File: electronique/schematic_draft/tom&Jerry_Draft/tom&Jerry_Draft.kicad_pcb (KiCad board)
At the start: 4 copper layers, 54 x 57 mm, 163 parts, among them IC1101 NCS199A2RSQT2G, IC301 TCA9555RTWR, IC901 NCS199A2RSQT2G, J1001 FTSH-105-01-F-DV-P-TR, J1301 Conn_01x02, J1401 Conn_01x02, J1501 Conn_01x02, J1601 Conn_01x02, J1601 Conn_02x05_Odd_FEMALE, J1602 Conn_02x05_Odd_FEMALE, J1603 Conn_02x05_Odd_FEMALE, J201 Interrupteur, J202 USB_C_Receptacle_USB2.0_16P, J203 Conn_01x02, J204 Conn_01x02, J301 Conn_01x08, J401 Conn_01x06, J402 Conn_01x06, J501 Conn_ST_STDC14, J601 Conn_01x03, J701 Conn_02x05_Odd_FEMALE, J701 FTSH-105-01-F-DV-P-TR, J702 Conn_02x05_Odd_FEMALE, J703 Conn_02x05_Odd_FEMALE, Q201 PMOS, SW501 SW_Push, SW502 SW_Push, SW503 SW_Push, U1101 ZXBM5210-S, U201 MP1475DJ-LF-P, U202 BQ25172DSGR, U301 ADXL343, U501 STM32G431CBU6, U601 PAM8302AAY, U801 LP5812ADSDR, U901 ZXBM5210-S, Y501 16MHz

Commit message: Corrections mineures routage - PCB V2.0
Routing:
- net /Périphériques/TOF3_GPIO1: track 2.00 -> 11.1 mm, vias 1 -> 2
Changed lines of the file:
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@@
 		(tags "resistor")
 		(property "Reference" "R206"
-			(at 0 -1.17 360)
+			(at 0 -1.17 0)
 			(layer "F.SilkS")
 			(effects
@@
 		)
 		(property "Value" "40.2k"
-			(at 0 1.17 360)
+			(at 0 1.17 0)
 			(layer "F.Fab")
 			(effects
@@
 		)
 		(fp_text user "${REFERENCE}"
-			(at 0 0 360)
+			(at 0 0 0)
 			(layer "F.Fab")
 			(effects
@@
 		(tags "capacitor")
 		(property "Reference" "C604"
-			(at 0 -1.43 360)
+			(at 0 -1.43 0)
 			(layer "F.SilkS")
 			(effects
@@
 		)
 		(fp_text user "${REFERENCE}"
-			(at 0 0 360)
+			(at 0 0 0)
 			(layer "F.Fab")
 			(effects
@@
 		(at 117.1 109.3)
 		(property "Reference" "U202"
-			(at 0.925 -2.385 360)
+			(at 0.925 -2.385 0)
 			(layer "F.SilkS")
 			(effects
@@
 		)
 		(property "Value" "BQ25172DSGR"
-			(at 6.64 2.385 360)
+			(at 6.64 2.385 0)
 			(layer "F.Fab")
 			(effects
@@
 		)
 		(property "Footprint" "Tom&Jerry:IC_BQ25172DSGR"
-			(at 0 0 360)
+			(at 0 0 0)
 			(layer "F.Fab")
 			(hide yes)
@@
 		)
 		(property "Datasheet" ""
-			(at 0 0 360)
+			(at 0 0 0)
 			(layer "F.Fab")
 			(hide yes)
@@
 		)
 		(property "Description" ""
-			(at 0 0 360)
+			(at 0 0 0)
 			(layer "F.Fab")
 			(hide yes)
@@
 		(tags "capacitor")
 		(property "Reference" "C605"
-			(at 0 -1.16 360)
+			(at 0 -1.16 0)
 			(layer "F.SilkS")
 			(effects
@@
 		)
 		(fp_text user "${REFERENCE}"
-			(at 0 0 360)
+			(at 0 0 0)
 			(layer "F.Fab")
 			(effects
@@
 		(tags "capacitor")
 		(property "Reference" "C211"
-			(at 0 -1.16 360)
+			(at 0 -1.16 0)
 			(layer "F.SilkS")
 			(effects
@@
 		)
 		(property "Value" "10n"
-			(at 0 1.16 360)
+			(at 0 1.16 0)
 			(layer "F.Fab")
 			(effects
@@
 		)
 		(fp_text user "${REFERENCE}"
-			(at 0 0 360)
+			(at 0 0 0)
 			(layer "F.Fab")
 			(effects
@@
 		(tags "resistor")
 		(property "Reference" "R208"
-			(at 0 -1.17 360)
+			(at 0 -1.17 0)
 			(layer "F.SilkS")
 			(effects
@@
 		)
 		(property "Value" "15k"
-			(at 0 1.17 360)
+			(at 0 1.17 0)
 			(layer "F.Fab")
 			(effects
@@
 		)
 		(fp_text user "${REFERENCE}"
-			(at 0 0 360)
+			(at 0 0 0)
 			(layer "F.Fab")
 			(effects
@@
 	)
 	(segment
+		(start 100.075158 62.949685)
+		(end 100.54 63.414527)
+		(width 0.2)
+		(layer "F.Cu")
+		(net 38)
+	)
+	(segment
 		(start 92.800001 65.148528)
 		(end 93.824266 64.124263)
@@
 	)
 	(segment
+		(start 100.54 63.414527)
+		(end 100.54 65.165)
+		(width 0.2)
+		(layer "F.Cu")
+		(net 38)
+	)
+	(segment
 		(start 92.800001 65.7)
 		(end 92.800001 65.148528)
@@
 		(net 38)
 	)
+	(via
+		(at 100.075158 62.949685)
+		(size 0.6)
+		(drill 0.3)
+		(layers "F.Cu" "B.Cu")
+		(net 38)
+	)
+	(segment
+		(start 94.107109 64.124263)
+		(end 93.824266 64.124263)
+		(width 0.2)
+		(layer "B.Cu")
+		(net 38)
+	)
+	(segment
+		(start 95.081687 63.149685)
+		(end 94.107109 64.124263)
+		(width 0.2)
+		(layer "B.Cu")
+		(net 38)
+	)
+	(segment
+		(start 100.075158 62.949685)
+		(end 99.875158 63.149685)
+		(width 0.2)
+		(layer "B.Cu")
+		(net 38)
+	)
+	(segment
+		(start 99.875158 63.149685)
+		(end 95.081687 63.149685)
+		(width 0.2)
+		(layer "B.Cu")
+		(net 38)
+	)
 	(segment
 		(start 98.960002 67.460002)
@@
 	)
 	(segment
-		(start 88.684744 71.275)
-		(end 87.4725 71.275)
+		(start 87.4025 71.275)
+		(end 86.4575 70.33)
 		(width 0.2)
 		(layer "F.Cu")
@@
 	)
 	(segment
-		(start 86.4575 70.26)
-		(end 86.4575 69.235)
+		(start 91.825 70.589937)
+		(end 90.614937 71.8)
 		(width 0.2)
 		(layer "F.Cu")
@@
 	)
 	(segment
-		(start 91.825 70.589937)
-		(end 90.614937 71.8)
+		(start 91.825 69.924937)
+		(end 91.825 70.589937)
 		(width 0.2)
 		(layer "F.Cu")
@@
 	)
 	(segment
-		(start 90.614937 71.8)
-		(end 89.209744 71.8)
+		(start 86.4575 70.33)
+		(end 86.4575 69.235)
 		(width 0.2)
 		(layer "F.Cu")
@@
 	)
 	(segment
-		(start 87.4725 71.275)
-		(end 86.4575 70.26)
+		(start 90.614937 71.8)
+		(end 89.209744 71.8)
 		(width 0.2)
 		(layer "F.Cu")
@@
 	)
 	(segment
-		(start 91.825 69.924937)
-		(end 91.825 70.589937)
+		(start 88.684744 71.275)
+		(end 87.4025 71.275)
 		(width 0.2)
 		(layer "F.Cu")
@@
 	)
 	(segment
-		(start 88.575 70.875)
-		(end 87.7275 70.0275)
+		(start 91.325 70.524251)
+		(end 90.449251 71.4)
 		(width 0.2)
 		(layer "F.Cu")
@@
 	)
 	(segment
-		(start 91.325 69.924937)
-		(end 91.325 70.524251)
+		(start 88.85043 70.875)
+		(end 87.975 70.875)
 		(width 0.2)
 		(layer "F.Cu")
@@
 	)
 	(segment
-		(start 88.85043 70.875)
-		(end 88.575 70.875)
+		(start 87.7275 70.6275)
+		(end 87.7275 69.235)
 		(width 0.2)
 		(layer "F.Cu")
@@
 	)
 	(segment
-		(start 89.37543 71.4)
-		(end 88.85043 70.875)
+		(start 91.325 69.924937)
+		(end 91.325 70.524251)
 		(width 0.2)
 		(layer "F.Cu")
@@
 	)
 	(segment
-		(start 91.325 70.524251)
-		(end 90.449251 71.4)
+		(start 90.449251 71.4)
+		(end 89.37543 71.4)
 		(width 0.2)
 		(layer "F.Cu")
@@
 	)
 	(segment
-		(start 90.449251 71.4)
-		(end 89.37543 71.4)
+		(start 89.37543 71.4)
+		(end 88.85043 70.875)
 		(width 0.2)
 		(layer "F.Cu")
@@
 	)
 	(segment
-		(start 91.35 69.575)
-		(end 91.35 70.239999)
+		(start 87.975 70.875)
+		(end 87.7275 70.6275)
 		(width 0.2)
 		(layer "F.Cu")
@@
 	)
 	(segment
-		(start 87.7275 70.0275)
-		(end 87.7275 69.235)
+		(start 91.35 69.575)
+		(end 91.35 70.239999)
 		(width 0.2)
 		(layer "F.Cu")
@@
 	)
 	(segment
-		(start 112.892892 69.907108)
-		(end 116.3 66.5)
-		(width 0.2)
-		(layer "F.Cu")
-		(net 76)
-	)
-	(segment
-		(start 125.01 65.9)
-		(end 125.7 66.59)
+		(start 106.607108 69.907108)
+		(end 112.892892 69.907108)
 		(width 0.2)
 		(layer "F.Cu")
@@
 	)
 	(segment
-		(start 119.72 66.5)
+		(start 119.82 66.4)
 		(end 120.32 65.9)
 		(width 0.2)
@@
 	)
 	(segment
-		(start 106.607108 69.907108)
-		(end 112.892892 69.907108)
+		(start 112.892892 69.907108)
+		(end 116.4 66.4)
 		(width 0.2)
 		(layer "F.Cu")
@@
 	)
 	(segment
-		(start 116.3 66.5)
-		(end 119.72 66.5)
+		(start 125.01 65.9)
+		(end 125.7 66.59)
+		(width 0.2)
+		(layer "F.Cu")
+		(net 76)
+	)
+	(segment
+		(start 116.4 66.4)
+		(end 119.82 66.4)
 		(width 0.2)
 		(layer "F.Cu")

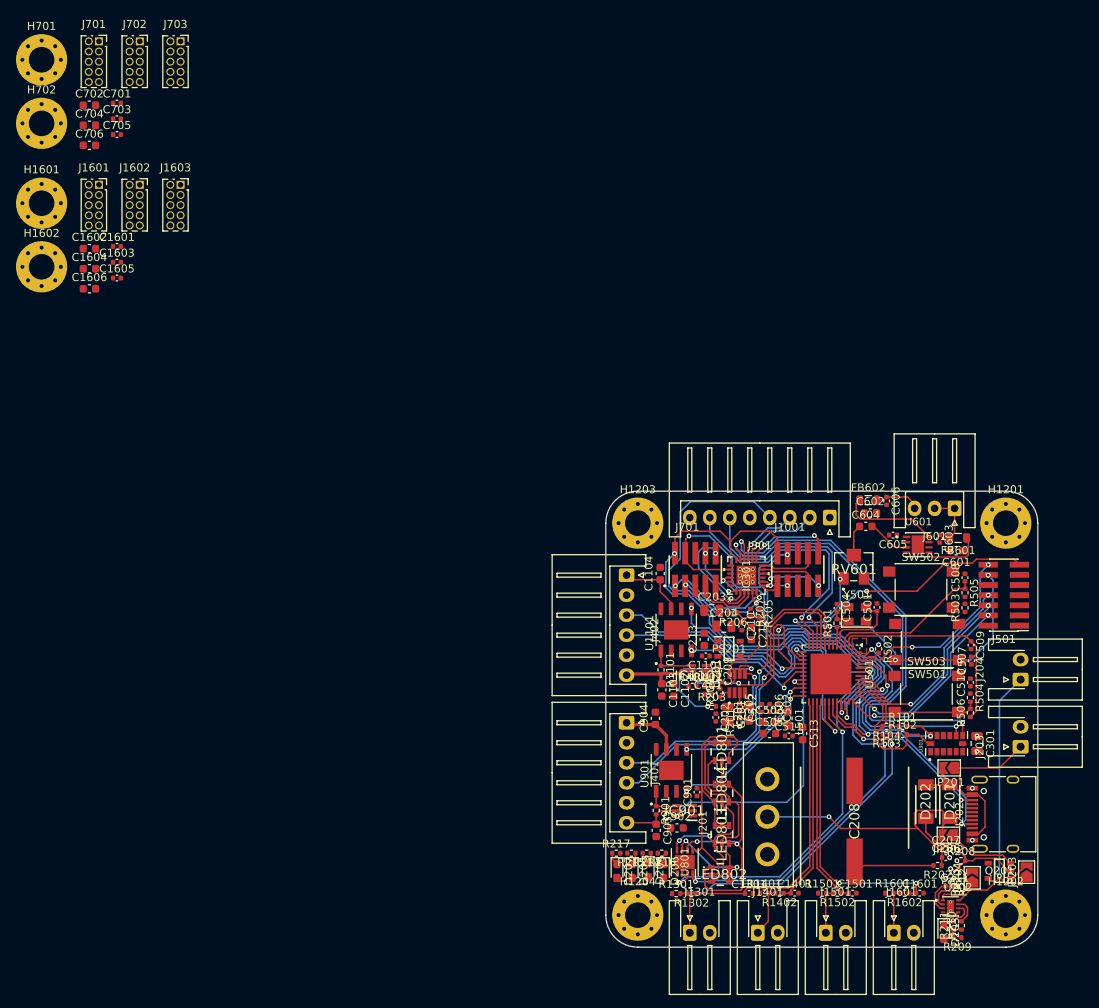
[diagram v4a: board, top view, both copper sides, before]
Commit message: Routage finish awaiting review PCB2.0
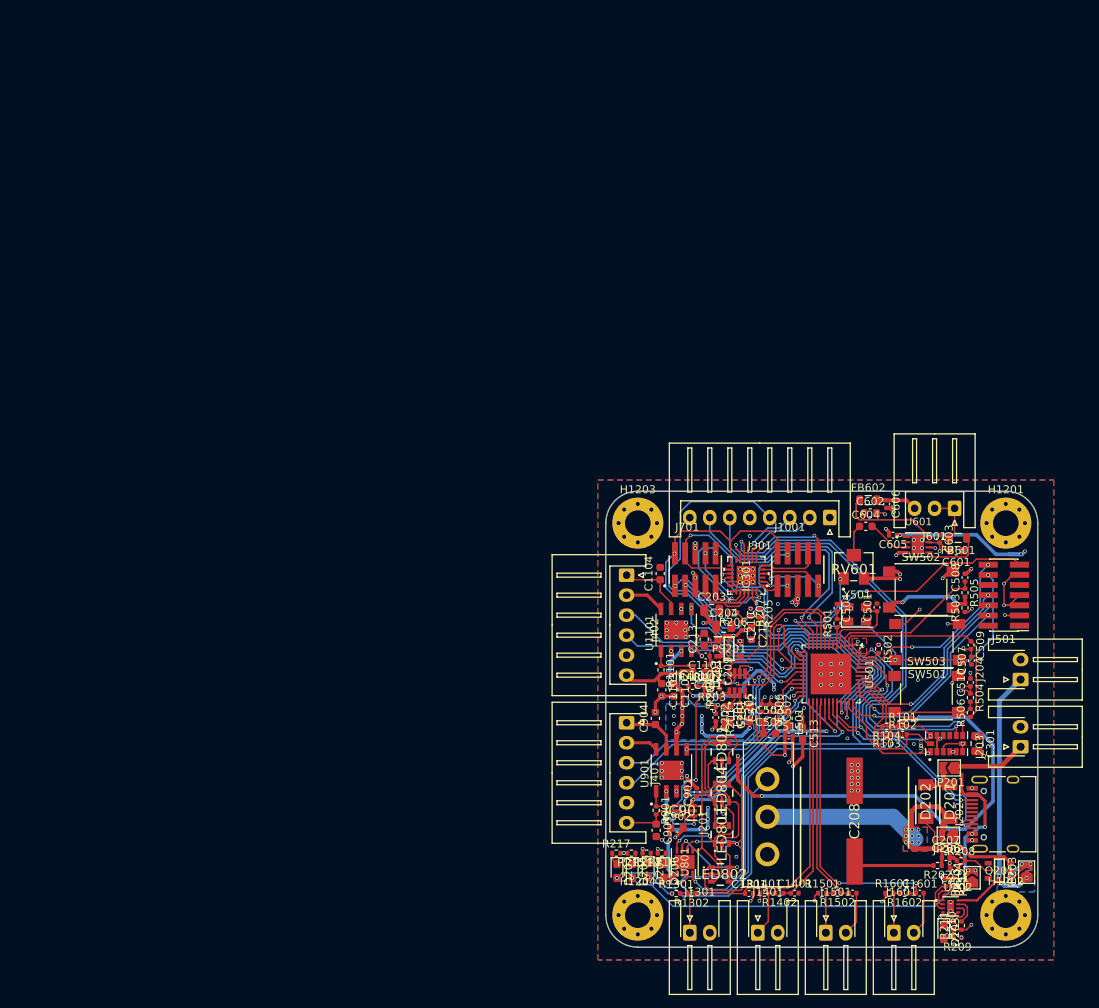
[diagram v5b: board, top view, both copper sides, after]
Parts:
- removed the C1601 at (12.9, 26.8)
- removed C1602, C1604, C1606, C702, C704, C706: 4.7uF, Capacitor_SMD:C_0603_1608Metric
- removed C1603, C1605, C701, C703, C705: 100nF, Capacitor_SMD:C_0402_1005Metric
- removed H1601, H1602, H701, H702: MountingHole_Pad, MountingHole:MountingHole_3.2mm_M3_Pad_Via
- removed the J1601 at (10.6, 19.1)
- removed J1602, J1603, J702, J703: Conn_02x05_Odd_FEMALE, Connector_PinSocket_1.27mm:PinSocket_2x05_P1.27mm_Vertical
- removed the J701 at (10.6, 1.18)
- moved C606 0.40 mm to (109.1, 59.0)
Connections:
- IC301 pad 25: (no net) -> GND
- IC301 pad V: (no net) -> GND
- U1101 pad 9: (no net) -> GND
- U601 pad 9: (no net) -> GND
- U901 pad 9: (no net) -> GND
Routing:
- net +5V: track 0.00 -> 124.4 mm, vias 0 -> 35
- net GND: track 0.00 -> 122.6 mm, vias 10 -> 104
- net +3.3V: track 0.00 -> 116.2 mm, vias 1 -> 28
- net /Alimentation/Batt_CHG: track 21.2 -> 73.0 mm, vias 0 -> 5
- net VCC: track 0.00 -> 48.6 mm, vias 0 -> 10
- net 1.65V: track 0.00 -> 25.4 mm, vias 0 -> 2
- net Net-(R503-Pad2): track 0.00 -> 12.1 mm, vias 0 -> 2
- net +3.3VA: track 2.41 -> 12.9 mm, vias 1 -> 0
- net /Motors&Drivers/ASSERV_I1: track 36.4 -> 30.5 mm
- net /Led_Debug/Led_Debug_SCL: track 148.2 -> 153.8 mm
- net /Led_Debug/Led_Debug_SDA: track 112.2 -> 117.6 mm
- net Net-(D201-K): track 35.7 -> 39.5 mm, vias 1 -> 9
- net Net-(JP203-B): track 2.69 -> 6.17 mm, vias 0 -> 3
- net /Périphériques/TOF4_GPIO1: track 12.7 -> 15.4 mm
- net /Motors&Drivers/ENCODER_2A: track 41.4 -> 40.0 mm
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- added copper zone on In2.Cu, net +3.3V
- added copper zone on B.Cu, net +5V
- added copper zone on F.Cu, net +5V
- added copper zone on In2.Cu, net +5V
- added copper zone on B.Cu, net /Alimentation/Batt_cell
- added copper zone on B.Cu, net GND
- added copper zone on F.Cu, net GND
- added copper zone on In1.Cu, net GND
- added copper zone on B.Cu, net Net-(D201-K)
- added copper zone on F.Cu, net Net-(D201-K)
- added copper zone on In2.Cu, net VCC

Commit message: c rémi qui m'a dit
g écrit sur le PCB.
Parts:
- added G***: LOGO, LOGO, B.Cu at (112.0, 95.5)
- added G***: LOGO, LOGO, B.Cu at (103.0, 102.5)
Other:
- board text added: "+"
- board text added: "-"
- board text added: "5V"
- board text added: "Batt"
- board text added: "Chr"
- board text added: "GND"
- board text added: "HP"
- board text added: "LIDAR"
- board text added: "Motor 1"
- board text added: "Motor 2"
- board text added: "Rst"
- board text added: "Réaliser par : R.Weidle R.Pace J.Thomasset"
- board text added: "ST"
- board text added: "Satch 3"
- board text added: "Stach 1"
- board text added: "Stach 2"
- board text added: "Stach 4"
- board text added: "Start"

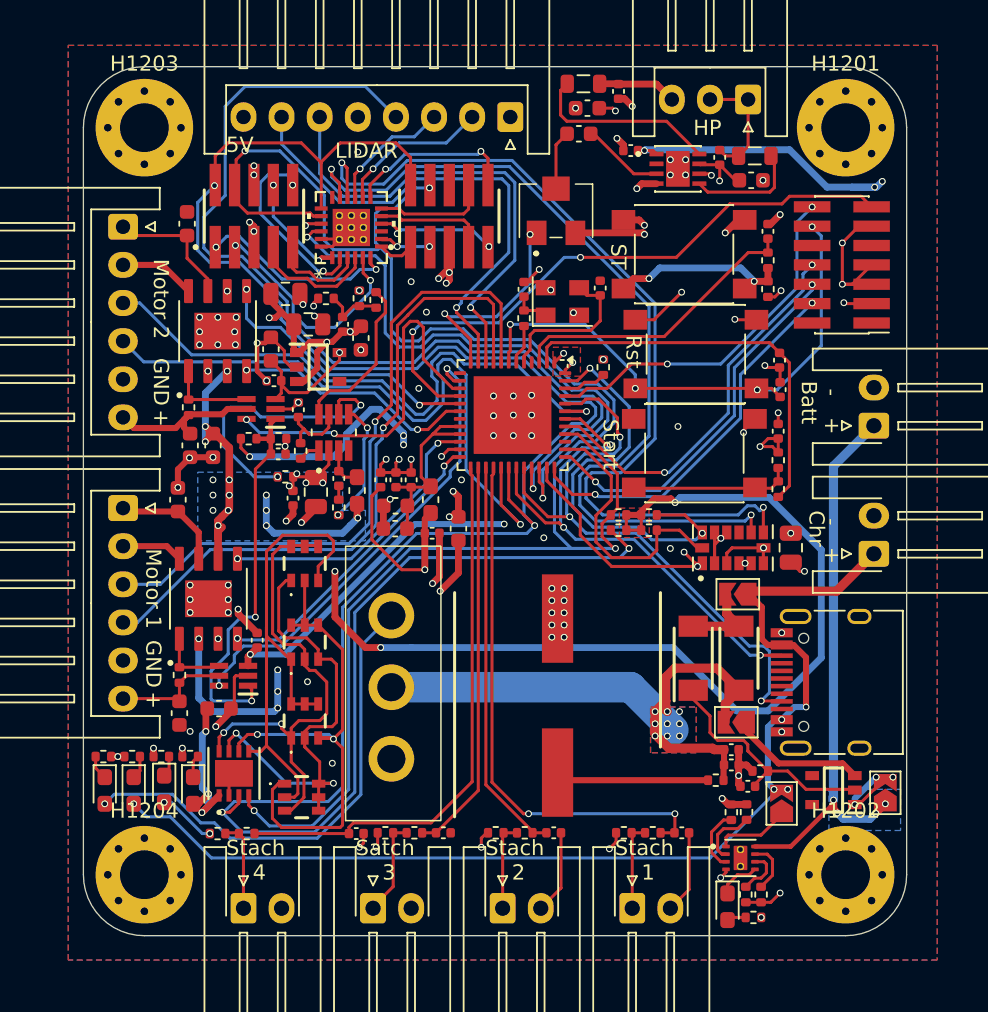
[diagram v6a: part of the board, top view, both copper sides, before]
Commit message: Kicad - Deplacement des pins sous PASTE x empreinte MOSFET
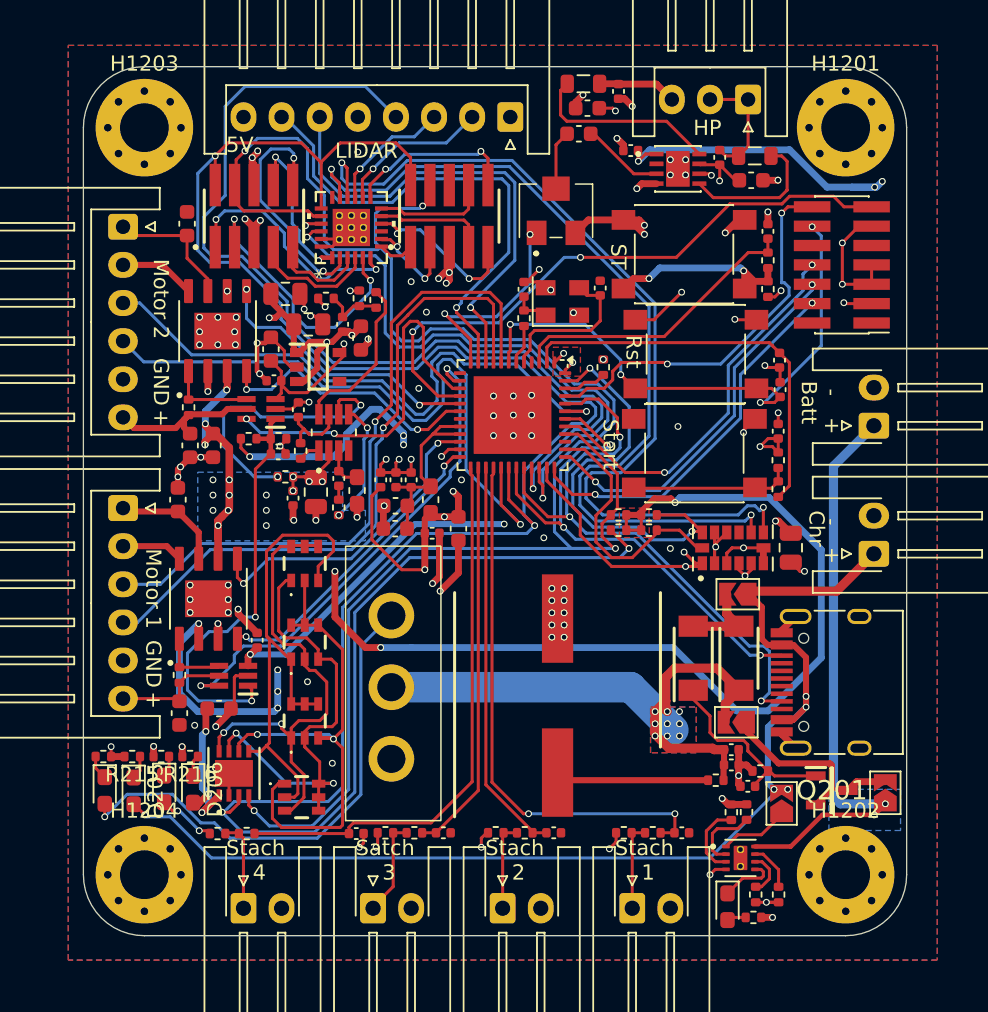
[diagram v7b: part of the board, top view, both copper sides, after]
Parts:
- Q201: value PMOS -> SI2365EDS-T1-GE3; footprint Tom&Jerry:SOT95P280X125-5N -> Tom&Jerry:SOT95P237X112-3N
- moved R210 1.15 mm to (119.6, 111.7)
- moved R211 0.65 mm to (118.1, 111.7)
- moved Q201 0.11 mm to (123.1, 104.9), turned to 0 degrees
- moved D206 0.08 mm to (81.2, 104.8)
- renumbered C1401 to C1501, C1501 to C1601, C1601 to C1701, J1401 to J1501, J1501 to J1601, J1601 to J1701, R1401 to R1501, R1402 to R1502, R1501 to R1601, R1502 to R1602, R1601 to R1701, R1602 to R1702
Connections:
- IC301 pad 25: GND -> (no net)
- IC301 pad V: GND -> (no net)
- Q201 pad 1: Net-(JP203-B) -> Net-(D202-K)
- Q201 pad 2: Net-(D202-K) -> Net-(JP202-A)
- Q201 pad 3: Net-(JP202-A) -> Net-(JP203-B)
- U1101 pad 9: GND -> (no net)
- U202 pad 10: GND -> (no net)
- U202 pad 11: GND -> (no net)
- U601 pad 9: GND -> (no net)
- U901 pad 9: GND -> (no net)
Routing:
- net VCC: track 48.6 -> 54.8 mm
- net +3.3V: track 116.2 -> 122.1 mm
- net GND: track 122.6 -> 117.9 mm, vias 104 -> 102
- net +5V: track 124.4 -> 120.5 mm
- net /Périphériques/TOF6_XSHUT: track 7.20 -> 10.8 mm
- net Net-(JP203-B): track 6.17 -> 2.70 mm, vias 3 -> 0
- net /Périphériques/TOF4_GPIO1: track 15.4 -> 18.9 mm
- net /Périphériques/TOF6_GPIO1: track 12.6 -> 15.8 mm
- net /Périphériques/TOF4_XSHUT: track 13.5 -> 16.5 mm
- net Net-(D202-K): track 15.9 -> 12.9 mm
- net /Périphériques/TOF1_GPIO1: track 3.31 -> 6.25 mm
- net /Alimentation/Batt_CHG: track 73.0 -> 75.6 mm
- net /Périphériques/TOF2_GPIO1: track 8.04 -> 10.7 mm
- net /Led_Debug/Led_Debug_SDA: track 117.6 -> 120.2 mm
- net 1.65V: track 25.4 -> 28.0 mm
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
